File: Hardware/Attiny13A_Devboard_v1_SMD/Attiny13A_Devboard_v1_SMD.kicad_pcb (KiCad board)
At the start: 2 copper layers, 48 x 24 mm, 20 parts, among them J1 Screw_Terminal_01x02, J2 ISP-6, J3 Conn_01x06_Pin, SW1 SW_RESET, U1 ATtiny13A-SS

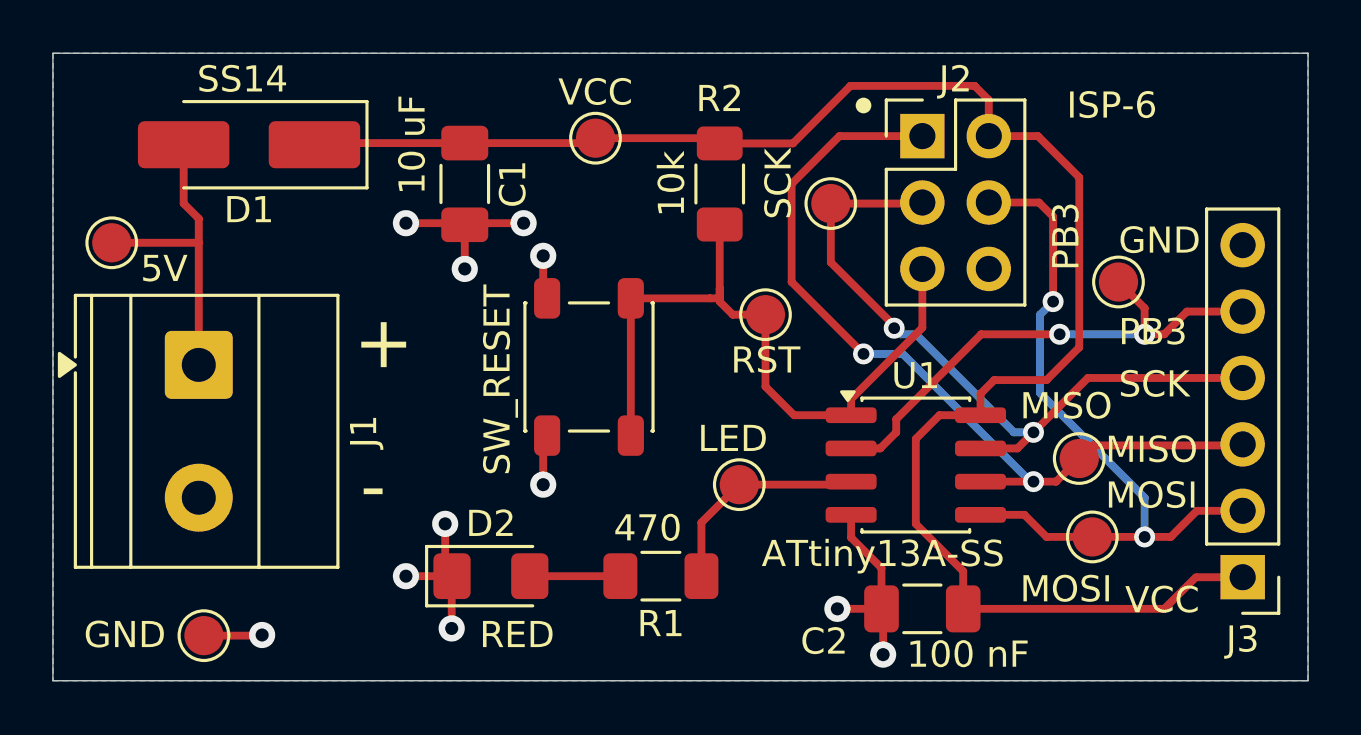
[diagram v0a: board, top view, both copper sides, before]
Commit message: Attiny13A Dev Board SMD - Updated Reset Switch Footprint for better Handsoldering - Optimized Silk Screen
Signed-off-by: alexanderjg85 <alexanderjg85@gmail.com>
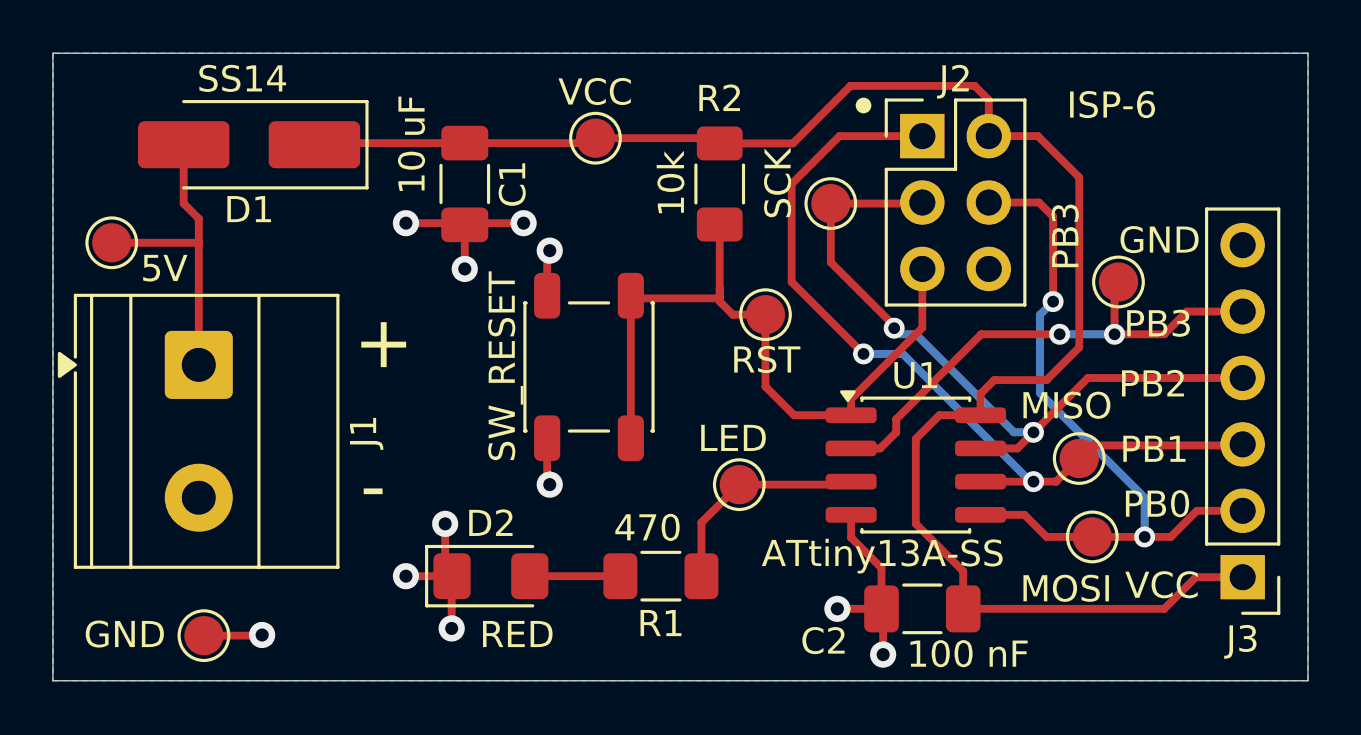
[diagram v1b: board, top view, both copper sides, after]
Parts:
- SW1: footprint Button_Switch_SMD:SW_SPST_PTS647_Sx38 -> AJ_Electromechanical:SW_SPST_PTS647_Sx38_Handsolder
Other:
- board text added: "PB0"
- board text added: "PB1"
- board text added: "PB2"
- board text removed: "MISO"
- board text removed: "MOSI"
- board text removed: "SCK"
